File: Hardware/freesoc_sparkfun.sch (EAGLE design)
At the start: 82 parts, among them J1 5.5x2.1mm Barrel, U1 CY8C5888AXI-LP096, U2 AP2202-ADJ, U3 AP2202-ADJ, U4 AP2202-ADJ, U5 AP2202-ADJ, U6 AP2202-ADJ, U7 CY8C5868LTI-LP039

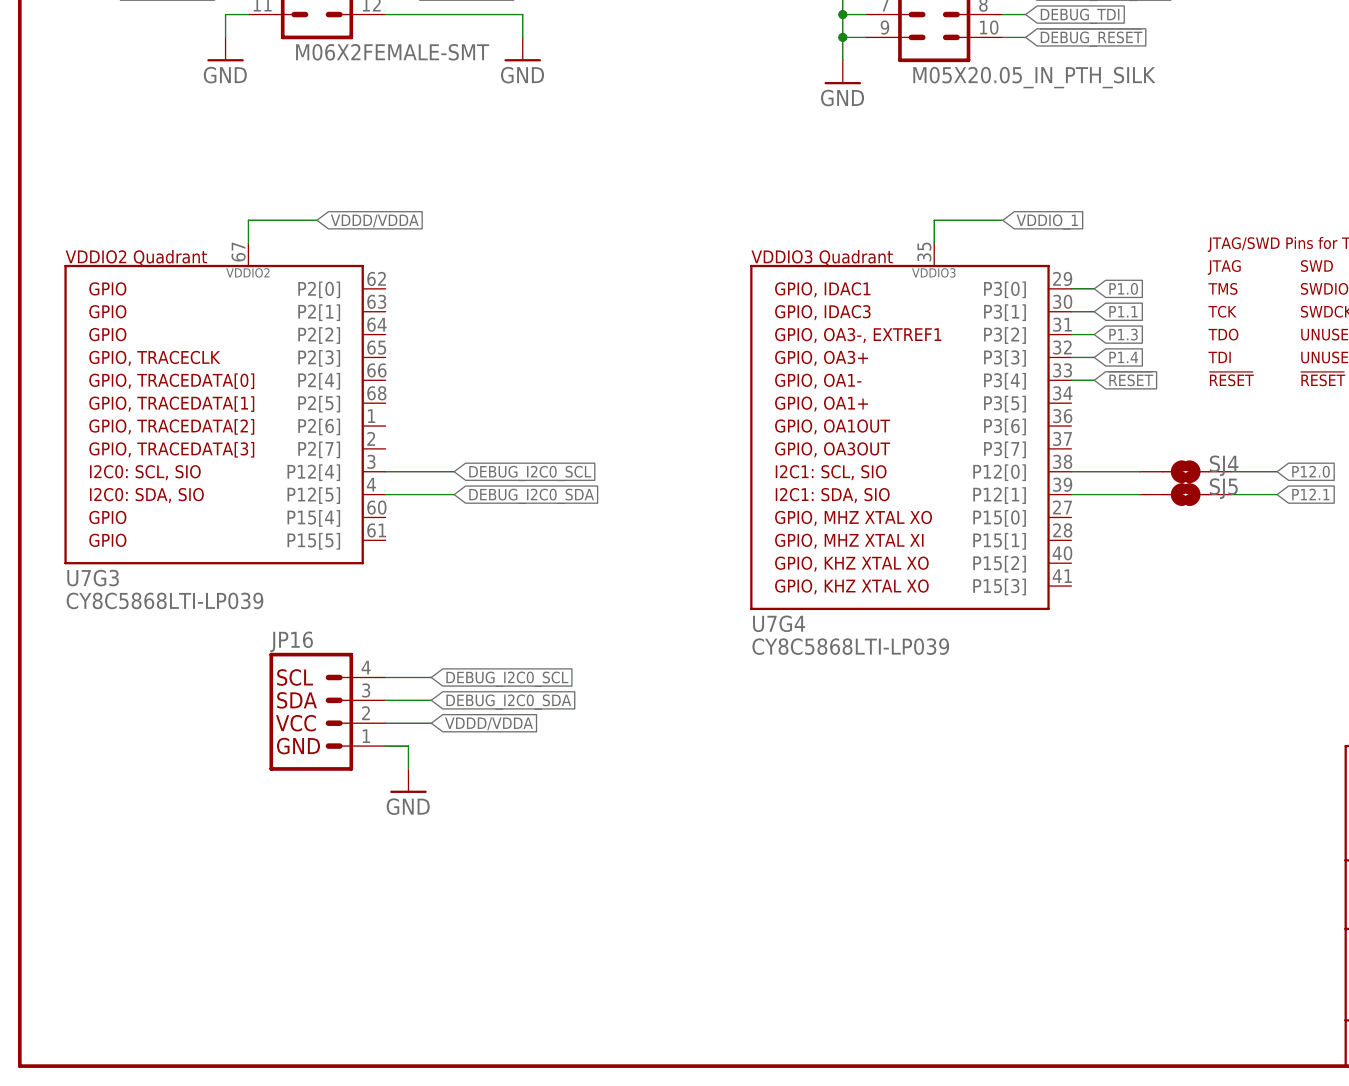
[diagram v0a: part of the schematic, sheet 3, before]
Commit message: Add some bypass caps
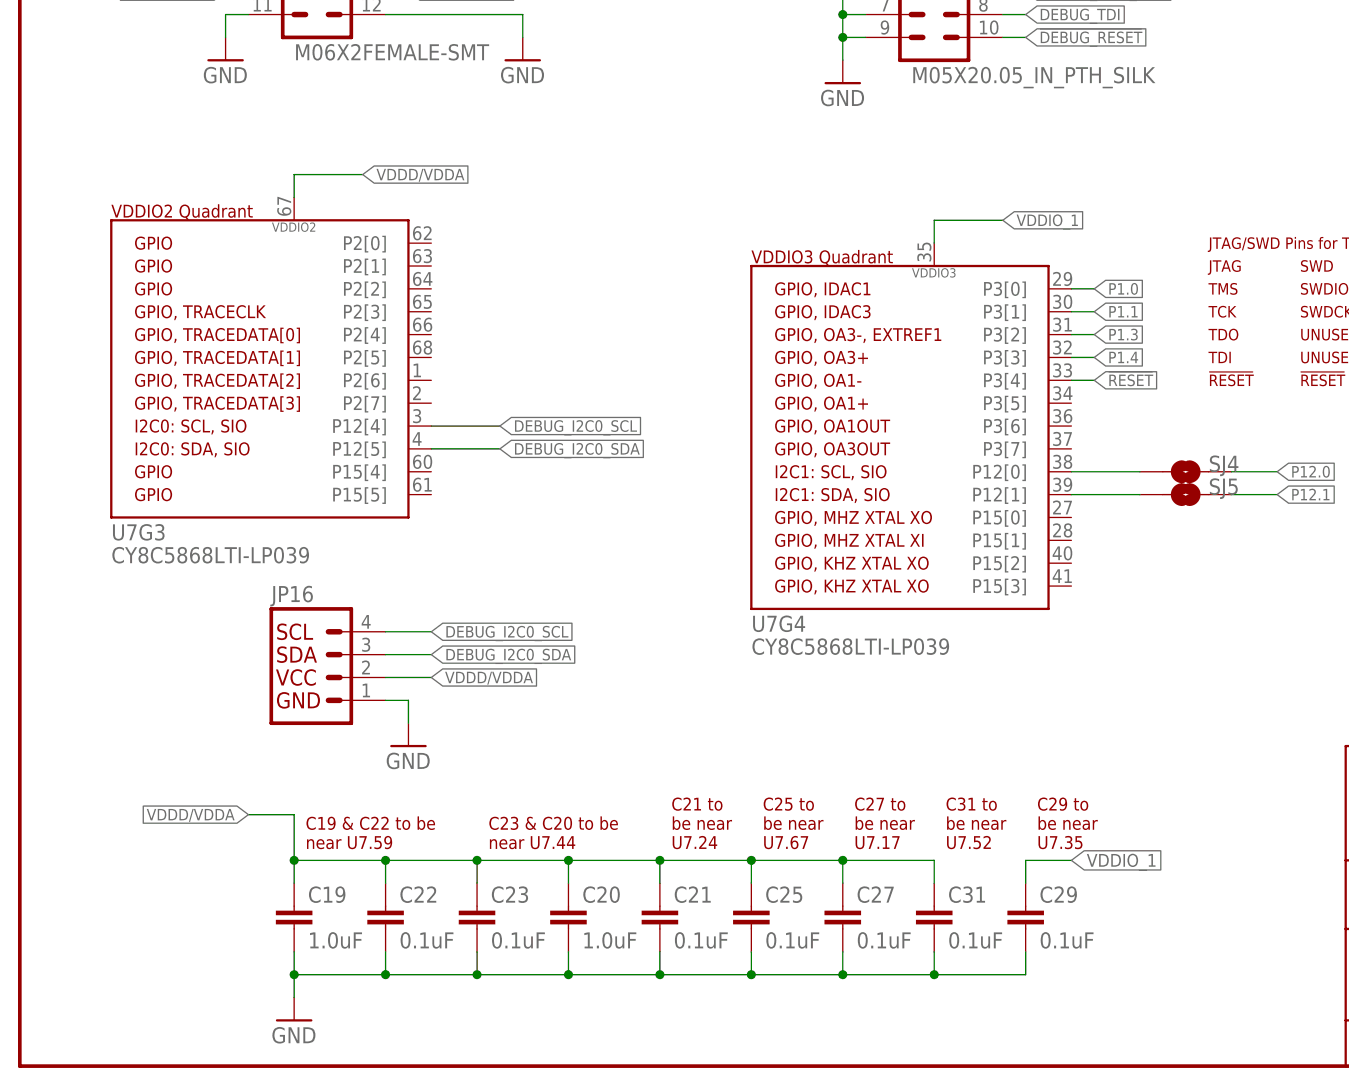
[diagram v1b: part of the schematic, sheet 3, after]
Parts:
- added C18: 2.2uF, SparkFun-Capacitors:2.2UF-10V-20%(0603)
- added C19, C20: 1.0uF, SparkFun-Capacitors:1.0UF-16V-10%(0603)
- added C21, C22, C23, C25, C27, C29, C31: 0.1uF, SparkFun-Capacitors:0.1UF-16V(+-10%)(0402)
- C13, C15: device SparkFun-Capacitors:0.1UF-25V(+80/-20%)(0603) -> SparkFun-Capacitors:0.1UF-16V(+-10%)(0402)
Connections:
- net N$1 renamed VCCA
- net N$10 renamed SW4
- net N$11 renamed SW3
- net N$12 renamed SW2
- net N$2 renamed ADJ2
- net N$20 renamed ADJ6
- net N$21 renamed SW6
- net N$4 renamed ADJ3
- net N$5 renamed ADJ4
- net N$7 renamed VCCD
- net N$8 renamed ADJ5
- net N$9 renamed SW5
- net GND: now also C18.2, C19.2, C20.2, C21.2, C22.2, C23.2, C25.2, C27.2, C29.2, C31.2, J1.GNDBREAK
- net VDDD/VDDA: now also C18.1, C19.1, C20.1, C21.1, C22.1, C23.1, C25.1, C27.1, C31.1
- net VDDIO_1: now also C29.1
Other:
- note added: "AGND and GND to be joined near ground pin of U6"
- note added: "C10 to be near U3 C11 to be near U1.100"
- note added: "C12 to be near U4 C13 to be near U1.26"
- note added: "C14 to be near U5 C15 to be near U1.75"
- note added: "C18 to be near U6"
- note added: "C19 & C22 to be near U7.59"
- note added: "C21 to be near U7.24"
- note added: "C23 & C20 to be near U7.44"
- note added: "C25 to be near U7.67"
- note added: "C27 to be near U7.17"
- note added: "C29 to be near U7.35"
- note added: "C31 to be near U7.52"
- note removed: "C8 to be near U3 C9 to be near U1.100"
- note removed: "C8 to be near U4 C9 to be near U1.26"
- note removed: "C8 to be near U5 C9 to be near U1.75"
- moved on the sheet: JP16, U7G3

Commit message: Routed, ready for review.
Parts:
- removed JP16, JP18: (no value), SparkFun-Connectors:I2C_STANDARD
- removed R1, R10, R13, R4, R7: 5.62k, SparkFun-Resistors:5.62KOHM1/10W1%(0603)
- removed R11, R14, R2, R5, R8: 3.40k, SparkFun-Resistors:3.40K-1/10W1%(0603)
- removed R12, R15, R3, R6, R9: 4.12k, SparkFun-Resistors:4.12K-1/10W1%(0603)
- removed SJ3: JUMPER-PAD-2-NC_BY_TRACE, SparkFun-Passives:JUMPER-PAD-2-NC_BY_TRACE
- removed SJ4, SJ5: JUMPER-PAD-2-NOYES_SILK, SparkFun-Passives:JUMPER-PAD-2-NOYES_SILK
- removed U$1: 4-POS-DIP, SparkFun-Electromechanical:4-POS-DIP
- removed U4, U5, U6: AP2202-ADJ, SparkFun-PowerIC:AP2202-ADJ
- added C24: 22pF, SparkFun-Capacitors:22PF-50V-5%(0603)
- added C26, C28: 2.2uF, SparkFun-Capacitors:2.2UF-10V-20%(0603)
- added S3, S4: (no value), SparkFun-Electromechanical:SWITCH-SPDTPTH
- added Y1: 32.768kHz, SparkFun-FreqCtrl:CRYSTALTC26H
- added Y2: (no value), SparkFun-FreqCtrl:CRYSTALHC49US
- C1, C16, C17, C19, C2, C20, C5, C7: device SparkFun-Capacitors:1.0UF-16V-10%(0603) -> SparkFun-Capacitors:1.0UF-16V-10%(0402)
- C10, C8: value 2.2uF -> 470pF; device SparkFun-Capacitors:2.2UF-10V-20%(0603) -> SparkFun-Capacitors:470PF-50V-5%(0603)SMD
- C11, C3, C4, C6, C9: device SparkFun-Capacitors:0.1UF-25V(+80/-20%)(0603) -> SparkFun-Capacitors:0.1UF-16V(+-10%)(0402)
- C12, C14: value 2.2uF -> (none); device SparkFun-Capacitors:2.2UF-10V-20%(0603) -> SparkFun-Capacitors:CAPPTH
- C18: value 2.2uF -> 22pF; device SparkFun-Capacitors:2.2UF-10V-20%(0603) -> SparkFun-Capacitors:22PF-50V-5%(0603)
- J1: value 5.5x2.1mm Barrel -> POWER_JACKPTH; device SparkFun-Connectors:POWER_JACKSMD -> SparkFun-Connectors:POWER_JACKPTH
- JP1, JP2: value USBSMD -> MicroB; device SparkFun-Connectors:USBSMD -> SparkFun-Connectors:USB_MICROB_PLUGCONN-11752
- JP10, JP11, JP12, JP15, JP8, JP9: value M06X2FEMALE-SMT -> 2X6 FEMALE; device SparkFun-Connectors:M06X2FEMALE-SMT -> SparkFun-Connectors:M06X2PTH_FEMALE
- JP13: device SparkFun-Connectors:M03X2SMT -> SparkFun-Connectors:M03X22X3_SILK_MALE_PTH
- JP4: device SparkFun-Connectors:M06SMD-STRAIGHT-COMBO-FEMALE -> SparkFun-Connectors:M06NO_SILK_FEMALE_PTH
- JP5, JP6: device SparkFun-Connectors:M08SMD-COMBO-FEMALE -> SparkFun-Connectors:M08NO_SILK_FEMALE_PTH
- JP7: value M10SMD_COMBO-FEMALE -> M10NO_SILK_PTH_FEMALE; device SparkFun-Connectors:M10SMD_COMBO-FEMALE -> SparkFun-Connectors:M10NO_SILK_PTH_FEMALE
- U1: value CY8C5888AXI-LP096 -> CY8C5868AXI-LP035
- U2: value AP2202-ADJ -> MIC5219 5V; device SparkFun-PowerIC:AP2202-ADJ -> SparkFun-PowerIC:V_REG_MIC52195V
- U3: value AP2202-ADJ -> MIC5219 3.3V; device SparkFun-PowerIC:AP2202-ADJ -> SparkFun-PowerIC:V_REG_MIC52193.3V
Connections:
- net DEBUG_D+ renamed DEBUG_D+_BUS
- net DEBUG_D- renamed DEBUG_D-_BUS
- net N$18 renamed PSOC_D+_PAD
- net N$19 renamed DEBUG_D-_PAD
- net N$22 renamed DEBUG_D+_PAD
- net N$3 renamed PSOC_D-_PAD
- net PSOC_D+ renamed PSOC_D+_BUS
- net PSOC_D- renamed PSOC_D-_BUS
- removed net ADJ2: R1.2, R2.1, R3.1, U2.ADJ
- removed net ADJ3: R4.2, R5.1, R6.1, U3.ADJ
- removed net ADJ4: R7.2, R8.1, R9.1, U4.ADJ
- removed net ADJ5: R10.2, R11.1, R12.1, U5.ADJ
- removed net ADJ6: R13.2, R14.1, R15.1, U6.ADJ
- removed net N$24: R20.1
- removed net N$31: SJ4.1, U7G4.P12[0]
- removed net N$32: SJ5.1, U7G4.P12[1]
- removed net SW2: R3.2, U$1.4A
- removed net SW3: R6.2, U$1.3A
- removed net SW4: R9.2, U$1.2A
- removed net SW5: R12.2, U$1.1A
- removed net SW6: R15.2, SJ3.1
- removed net VDDD/VDDA: C18.1, C19.1, C2.1, C20.1, C21.1, C22.1, C23.1, C25.1, C27.1, C3.1, C31.1, C4.1, C5.1, C6.1, JP14.1, JP15.10, JP15.9, JP16.2, JP6.4, JP6.5, R13.1, U1G5.VDDA, U1G5.VDDD0, U1G5.VDDD1, U6.OUT, U7G1.VDDIO0, U7G2.VDDIO1, U7G3.VDDIO2, U7G5.VDDA, U7G5.VDDD0, U7G5.VDDD1
- removed net VDDIO_0: C14.1, C15.1, JP8.10, JP8.9, JP9.10, JP9.9, R10.1, U1G1.VDDIO0, U5.OUT
- removed net VDDIO_1: C12.1, C13.1, C29.1, JP10.10, JP10.9, JP11.10, JP11.9, JP17.1, R7.1, U1G2.VDDIO1, U4.OUT, U7G4.VDDIO3
- removed net VDDIO_2: C10.1, C11.1, JP13.2, JP6.7, R4.1, U1G3.VDDIO2, U3.OUT
- removed net VDDIO_3: C8.1, C9.1, JP12.10, JP12.9, JP18.2, R1.1, U1G4.VDDIO3, U2.OUT
- new net 3.3V: C26.2, JP6.5, S3.S, S4.S, U3.OUT
- new net 5V: C20.1, C23.1, C28.2, C5.1, C6.1, JP6.4, S3.O, S4.O, U1G5.VDDA, U2.OUT, U7G5.VDDA
- new net DEBUG_LED: R20.1, U7G3.P2[0]
- new net N$1: C8.1, U3.BP
- new net N$2: C10.1, U2.BP
- new net VDDIO: C13.1, C15.1, C19.1, C2.1, C21.1, C22.1, C25.1, C27.1, C29.1, C3.1, C31.1, C4.1, C9.1, JP10.10, JP10.9, JP11.10, JP11.9, JP12.10, JP12.9, JP14.1, JP15.10, JP15.9, JP17.1, JP8.10, JP8.9, JP9.10, JP9.9, S4.P, U1G1.VDDIO0, U1G2.VDDIO1, U1G4.VDDIO3, U1G5.VDDD0, U1G5.VDDD1, U7G1.VDDIO0, U7G2.VDDIO1, U7G3.VDDIO2, U7G4.VDDIO3, U7G5.VDDD0, U7G5.VDDD1
- new net VDDIO_ARDUINO: C11.1, JP13.2, JP6.7, S3.P, U1G3.VDDIO2
- net A0: now also U1G3.P15[5]; no longer U1G3.P6[0]
- net A1: now also U1G3.P15[4]; no longer U1G3.P6[1]
- net A2: now also U1G3.P6[3]; no longer U1G3.P6[2]
- net A3: now also U1G3.P6[2]; no longer U1G3.P6[3]
- net A4: now also U1G3.P6[1]; no longer U1G3.P15[4]
- net A5: now also U1G3.P6[0]; no longer U1G3.P15[5]
- net AGND: now also C17.2, C20.2, C23.2, U7G5.VSSA
- net D0: now also U1G3.P2[0]; no longer U1G3.P2[4]
- net D1: now also U1G3.P2[1]; no longer U1G3.P2[5]
- net D10: now also U1G3.P6[4]; no longer U1G3.P2[6]
- net D11: now also U1G3.P6[5]; no longer U1G3.P6[6]
- net D12: now also U1G3.P6[6]; no longer U1G3.P6[5]
- net D2: now also U1G3.P2[2]; no longer U1G3.P2[3]
- net D3: now also U1G3.P2[3]; no longer U1G3.P12[5]
- net D4: now also U1G3.P2[4]; no longer U1G3.P2[0]
- net D5: now also U1G3.P2[5]; no longer U1G3.P6[4]
- net D6: now also U1G3.P2[6]; no longer U1G3.P2[7]
- net D7: now also U1G3.P2[7]; no longer U1G3.P2[2]
- net D8: now also U1G3.P12[4]; no longer U1G3.P2[1]
- net D9: now also U1G3.P12[5]; no longer U1G3.P12[4]
- net DEBUG_I2C0_SCL: no longer JP16.4
- net DEBUG_I2C0_SDA: no longer JP16.3
- net GND: now also C24.2, C26.1, C28.1, JP1.SHIELD, JP2.SHIELD; no longer C17.2, C20.2, C23.2, JP16.1, JP18.1, R11.2, R14.2, R2.2, R5.2, R8.2, SJ3.2, U$1.1B, U$1.2B, U$1.3B, U$1.4B, U4.GND, U5.GND, U6.GND, U7G5.VSSA
- net N$15: now also JP1.VCC; no longer JP1.VBUS
- net P12.0: no longer JP18.4, SJ4.2
- net P12.1: no longer JP18.3, SJ5.2
- net P15.0: now also C14.1, Y2.1
- net P15.1: now also C12.1, Y2.2
- net P15.2: now also C18.1, Y1.2
- net P15.3: now also C24.1, Y1.1
- net P4.0: now also JP9.2; no longer JP9.1
- net P4.1: now also JP9.1; no longer JP9.2
- net P4.2: now also JP9.4; no longer JP9.3
- net P4.3: now also JP9.3; no longer JP9.4
- net P4.4: now also JP9.6; no longer JP9.5
- net P4.5: now also JP9.5; no longer JP9.6
- net P4.6: now also JP9.8; no longer JP9.7
- net P4.7: now also JP9.7; no longer JP9.8
- net P5.0: now also JP11.2; no longer JP11.1
- net P5.1: now also JP11.1; no longer JP11.2
- net P5.2: now also JP11.4; no longer JP11.3
- net P5.3: now also JP11.3; no longer JP11.4
- net P5.4: now also JP11.6; no longer JP11.5
- net P5.5: now also JP11.5; no longer JP11.6
- net P5.6: now also JP11.8; no longer JP11.7
- net P5.7: now also JP11.7; no longer JP11.8
- net V_DEBUG: now also JP2.VCC; no longer JP2.VBUS
- net V_IN: no longer U4.EN, U4.IN, U5.EN, U5.IN, U6.EN, U6.IN
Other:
- note added: "AGND and GND to be joined near ground pin of U2"
- note added: "C11 to be near U1.100"
- note added: "C13 to be near U1.26"
- note added: "C15 to be near U1.75"
- note added: "C16 near U7.26 or U7.57"
- note added: "C17 near U7.26 or U7.42"
- note added: "C26 to be near U3 output"
- note added: "C28 to be near U2 output"
- note added: "C9 to be near U1.50"
- note added: "Minimize trace len between U7.26 and U7.57"
- note added: "VDDA *must* be the highest voltage supply on the chip. VDDD might as well be, too. No need to change them."
- note added: "Y2, C12 and C14 are all DNP"
- note removed: "AGND and GND to be joined near ground pin of U6"
- note removed: "C10 to be near U3 C11 to be near U1.100"
- note removed: "C12 to be near U4 C13 to be near U1.26"
- note removed: "C14 to be near U5 C15 to be near U1.75"
- note removed: "C18 to be near U6"
- note removed: "C8 to be near U2 C9 to be near U1.50"
- note removed: "Provide separate traces for VDDA and VDDD, joined at regulator"
- note removed: "This section is tied to VDDIO 0."
- note removed: "This section is tied to VDDIO 1."
- note removed: "This section is tied to VDDIO 3."
- moved on the sheet: C10, C11, C13, C15, C16, C17, C20, C21, C23, C25, C27, C29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

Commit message: Routed, with board checklist.
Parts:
- removed PT1: 2PT_GND_TIE, SparkFun-Passives:2PT_GND_TIE
- added C30, C32, C33, C34, C35, C36: 0.1uF, SparkFun-Capacitors:0.1UF-16V(+-10%)(0402)
- added FID1, FID2: FIDUCIAL1X2, SparkFun-Aesthetics:FIDUCIAL1X2
- added LOGO1: SFE_LOGO_NAME_FLAME.2_INCH, SparkFun-Aesthetics:SFE_LOGO_NAME_FLAME.2_INCH
- added LOGO2: OSHW-LOGOS, SparkFun-Aesthetics:OSHW-LOGOS
- added S5, S6: SWITCH-MOMENTARY-2SMD, SparkFun-Electromechanical:SWITCH-MOMENTARY-2SMD
- added SJ3, SJ4, SJ5: JUMPER-PAD-2-NO, SparkFun-Passives:JUMPER-PAD-2-NO
- added STANDOFF1, STANDOFF2, STANDOFF3, STANDOFF4: STAND-OFF, SparkFun-Electromechanical:STAND-OFF
- added U$1: FOUR_LAYER_WARNING, SparkFun-Aesthetics:FOUR_LAYER_WARNING
- C4: value 0.1uF -> 1.0uF; device SparkFun-Capacitors:0.1UF-16V(+-10%)(0402) -> SparkFun-Capacitors:1.0UF-16V-10%(0402)
- JP10: value 2X6 FEMALE -> (none); device SparkFun-Connectors:M06X2PTH_FEMALE -> SparkFun-Connectors:M08SILK_FEMALE_PTH
- JP4: device SparkFun-Connectors:M06NO_SILK_FEMALE_PTH -> SparkFun-Connectors:M06SILK_FEMALE_PTH
- JP5, JP6: device SparkFun-Connectors:M08NO_SILK_FEMALE_PTH -> SparkFun-Connectors:M08SILK_FEMALE_PTH
- JP7: value M10NO_SILK_PTH_FEMALE -> M10SILK_FEMALE_PTH; device SparkFun-Connectors:M10NO_SILK_PTH_FEMALE -> SparkFun-Connectors:M10SILK_FEMALE_PTH
- R16, R17, R18, R19: device SparkFun-Resistors:22OHM1/10W1%(0603) -> SparkFun-Resistors:22OHM1/10W1%(0402)
- R20, R21: value 330 -> 1K; device SparkFun-Resistors:330OHM1/10W1%(0603) -> SparkFun-Resistors:1KOHM1/10W1%(0603)
- SJ1: value JUMPER-PAD-2-NC_BY_TRACE -> JUMPER-PAD-2-NC_BY_PASTE; device SparkFun-Passives:JUMPER-PAD-2-NC_BY_TRACE -> SparkFun-Passives:JUMPER-PAD-2-NC_BY_PASTE
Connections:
- removed net AGND: C1.2, C17.2, C20.2, C23.2, C5.2, C6.2, PT1.P$1, U1G5.VSSA, U7G5.VSSA
- removed net DEBUG_I2C0_SCL: U7G3.P12[4]
- removed net DEBUG_I2C0_SDA: U7G3.P12[5]
- removed net DEBUG_P0.2: JP15.3, U7G1.P0[2]
- removed net DEBUG_P0.3: JP15.4, U7G1.P0[3]
- removed net DEBUG_P0.4: JP15.5, U7G1.P0[4]
- removed net DEBUG_P0.5: JP15.6, U7G1.P0[5]
- removed net DEBUG_P0.6: JP15.7, U7G1.P0[6]
- removed net DEBUG_P0.7: JP15.8, U7G1.P0[7]
- new net DEBUG_DS_BP: C30.1, U7G1.P0[3]
- new net DEBUG_P1.2: JP15.2, U7G2.P1[2]
- new net DEBUG_P12.6: JP15.9, U7G2.P12[6]
- new net DEBUG_P12.7: JP15.10, U7G2.P12[7]
- new net DEBUG_P3.0: JP15.12, U7G4.P3[0]
- new net DEBUG_P3.4: JP15.5, U7G4.P3[4]
- new net DEBUG_P3.5: JP15.6, U7G4.P3[5]
- new net DEBUG_P3.6: JP15.7, U7G4.P3[6]
- new net DEBUG_P3.7: JP15.8, U7G4.P3[7]
- new net DEBUG_SAR0_BP: C33.1, U7G1.P0[4]
- new net DEBUG_SAR1_BP: C32.1, U7G1.P0[2]
- new net DEBUG_USER_BTN: S5.1, U7G2.P1[6]
- new net N$3: C34.1, SJ5.2
- new net N$4: C35.1, SJ4.2
- new net N$5: C36.1, SJ3.2
- net !RESET: now also U7G3.P2[4]; no longer U7G4.P3[4]
- net DEBUG_LED: now also U7G4.P3[1]; no longer U7G3.P2[0]
- net DEBUG_P0.0: now also JP15.3; no longer JP15.1
- net DEBUG_P0.1: now also JP15.4; no longer JP15.2
- net GND: now also C1.2, C17.2, C20.2, C23.2, C30.2, C32.2, C33.2, C34.2, C35.2, C36.2, C5.2, C6.2, JP10.2, S5.2, S6.2, U1G5.VSSA, U7G5.VSSA; no longer JP10.11, JP10.12, JP15.12, PT1.P$2
- net P0.2: now also SJ3.1
- net P0.3: now also SJ4.1
- net P0.4: now also SJ5.1
- net P1.0: now also U7G3.P2[0]; no longer JP10.1, U7G4.P3[0]
- net P1.1: now also U7G3.P2[1]; no longer JP10.2, U7G4.P3[1]
- net P1.2: now also S6.1; no longer JP10.3
- net P1.3: no longer JP10.4, U7G4.P3[2]
- net P1.4: no longer JP10.5, U7G4.P3[3]
- net P1.5: no longer JP10.6
- net P1.6: no longer JP10.7
- net P1.7: no longer JP10.8
- net P12.0: now also JP10.3
- net P12.1: now also JP10.4
- net P12.2: now also JP10.5
- net P12.3: now also JP10.6
- net P12.6: now also JP10.7
- net P12.7: now also JP10.8
- net VDDIO: now also JP10.1, JP15.1; no longer JP10.10, JP10.9, JP15.10, JP15.9
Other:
- note added: "01"
- note added: "ADC Ref Bypass Caps"
- note added: "Close to bypass diode for low-V battery operation"
- note added: "DEBUG I/O Quadrants"
- note added: "DS Bypass"
- note added: "Debug Bypass/Decouple Caps"
- note added: "Debug Power Pins"
- note added: "Debug User I/O"
- note added: "Developed with help from Jon Moeller and Cypress Semiconductor"
- note added: "JP3 is DNP"
- note added: "M. Hord"
- note added: "Open to isolate USB/Barrel from Power supply"
- note added: "Port 12 (SIO pins)"
- note added: "Power Supply"
- note added: "Power Supply 2.5V - 12V"
- note added: "Quadrant 0"
- note added: "Quadrant 1"
- note added: "Quadrant 2"
- note added: "Quadrant 3"
- note added: "SAR0 Bypass"
- note added: "SAR1 Bypass"
- note added: "SJ3, SJ4, and SJ5 ship open. Close them if you want to bypass the ADC refs for better ADC performance."
- note added: "SWD Pins to Target PSoC5LP"
- note added: "Target"
- note added: "Target Device Decouple/Bypass Caps"
- note added: "Target Supply Pins"
- note added: "This section conforms to the Arduino Uno R3 layout conventions."
- note removed: "AGND and GND to be joined near ground pin of U2"
- note removed: "JTAG"
- note removed: "JTAG/SWD Pins for Target PSoC5LP"
- note removed: "PSOC 5LP"
- note removed: "SWD"
- note removed: "TCK"
- note removed: "TDI"
- note removed: "TDO"
- note removed: "TMS"
- note removed: "This section conforms to the Arduino Uno R3 layout conventions. It is tied to VDDIO 2."
- note removed: "UNUSED"
- note removed: "VDDA *must* be the highest voltage supply on the chip. VDDD might as well be, too. No need to change them."
- moved on the sheet: C10, C19, C20, C21, C22, C23, C25, C26, C27, C28, C29, C31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

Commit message: Fixed stuff from QC spreadsheet review.
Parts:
- JP10: value (none) -> 1x8 FEMALE PTH
- JP11, JP12, JP15, JP8, JP9: value 2X6 FEMALE -> 2X6 FEMALE PTH
- JP14, JP17: value M05X20.05_IN_PTH_SILK -> DNP
- JP4: value (none) -> 1X6 FEMALE PTH
- JP5, JP6: value (none) -> 1X8 FEMALE PTH
- JP7: value M10SILK_FEMALE_PTH -> 1X10 FEMALE PTH
- S1, S2, S5, S6: value SWITCH-MOMENTARY-2SMD -> SPST-MOM
- S3, S4: value (none) -> SPDT
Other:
- note added: "USER BUTTON"
- note added: "USER LED"
- moved on the sheet: S6
